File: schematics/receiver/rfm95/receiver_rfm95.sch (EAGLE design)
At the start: 47 parts, among them IC1 ATMEGA328P, Q1 16MHz, Q2 BC817-16SMD, U1 RFM95_LORA_MODULE, U2 AMS1117_3.3

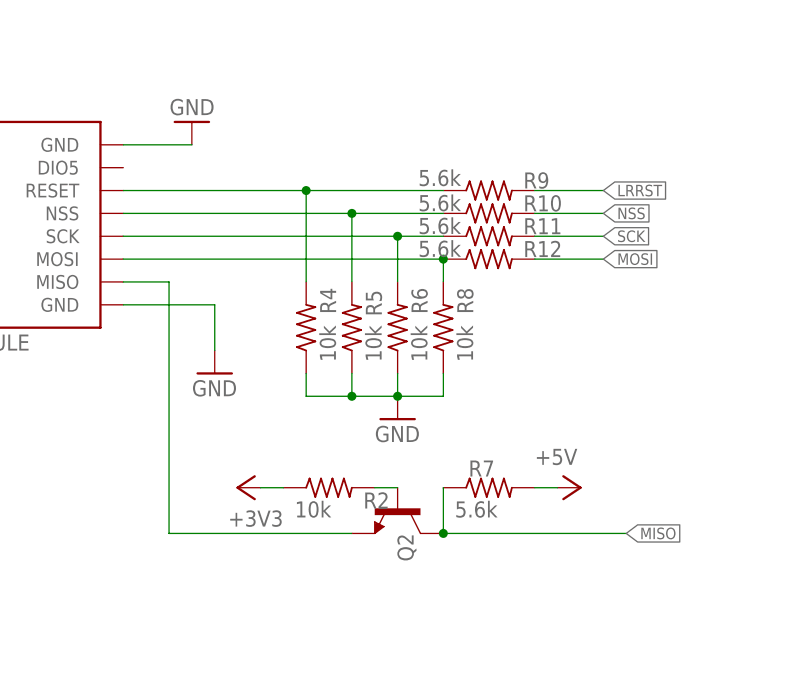
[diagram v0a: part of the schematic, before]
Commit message: Fixed incorrect resistor values
- Fixed incorrect resistor values in the level shifters.
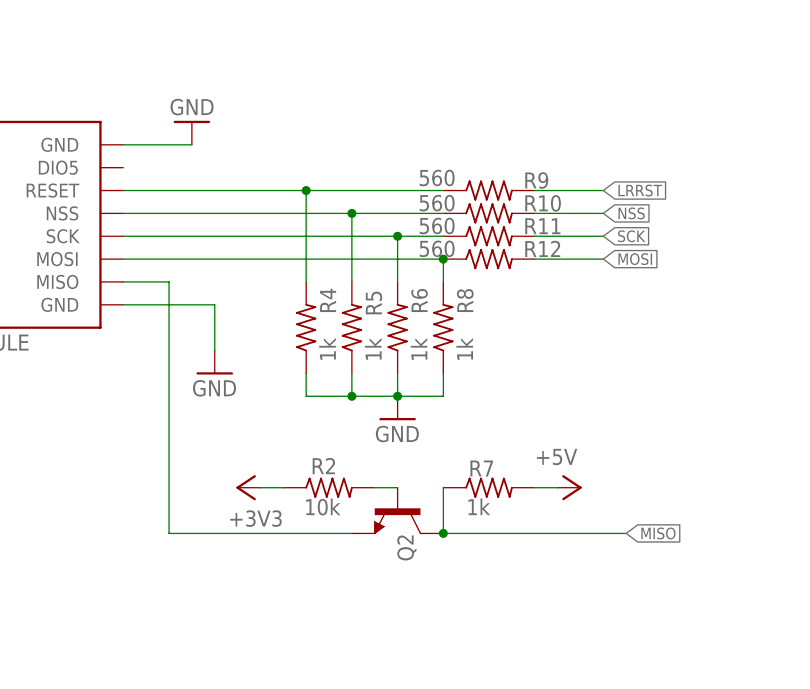
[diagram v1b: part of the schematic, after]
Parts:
- R10, R11, R12, R9: value 5.6k -> 560
- R4, R5, R6, R8: value 10k -> 1k
- R7: value 5.6k -> 1k
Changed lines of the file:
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@@
 <part name="P+9" library="supply1" deviceset="+5V" device=""/>
 <part name="P+4" library="supply1" deviceset="+5V" device=""/>
-<part name="R9" library="rcl" deviceset="R-US_" device="R0805" value="5.6k"/>
-<part name="R10" library="rcl" deviceset="R-US_" device="R0805" value="5.6k"/>
-<part name="R11" library="rcl" deviceset="R-US_" device="R0805" value="5.6k"/>
-<part name="R12" library="rcl" deviceset="R-US_" device="R0805" value="5.6k"/>
-<part name="R8" library="rcl" deviceset="R-US_" device="R0805" value="10k"/>
-<part name="R6" library="rcl" deviceset="R-US_" device="R0805" value="10k"/>
-<part name="R5" library="rcl" deviceset="R-US_" device="R0805" value="10k"/>
-<part name="R4" library="rcl" deviceset="R-US_" device="R0805" value="10k"/>
+<part name="R9" library="rcl" deviceset="R-US_" device="R0805" value="560"/>
+<part name="R10" library="rcl" deviceset="R-US_" device="R0805" value="560"/>
+<part name="R11" library="rcl" deviceset="R-US_" device="R0805" value="560"/>
+<part name="R12" library="rcl" deviceset="R-US_" device="R0805" value="560"/>
+<part name="R8" library="rcl" deviceset="R-US_" device="R0805" value="1k"/>
+<part name="R6" library="rcl" deviceset="R-US_" device="R0805" value="1k"/>
+<part name="R5" library="rcl" deviceset="R-US_" device="R0805" value="1k"/>
+<part name="R4" library="rcl" deviceset="R-US_" device="R0805" value="1k"/>
 <part name="GND8" library="supply1" deviceset="GND" device=""/>
 <part name="P+8" library="supply1" deviceset="+5V" device=""/>
 <part name="P+7" library="supply1" deviceset="+5V" device=""/>
 <part name="Q2" library="transistor-npn" deviceset="BC817*" device="SMD" technology="-16" value=""/>
-<part name="R7" library="rcl" deviceset="R-US_" device="R0805" value="5.6k"/>
+<part name="R7" library="rcl" deviceset="R-US_" device="R0805" value="1k"/>
 <part name="R2" library="rcl" deviceset="R-US_" device="R0805" value="10k"/>
 <part name="+3V32" library="supply1" deviceset="+3V3" device=""/>
@@
 <instance part="R7" gate="G$1" x="93.98" y="-35.56" smashed="yes">
 <attribute name="NAME" x="91.694" y="-34.3154" size="1.778" layer="95"/>
-<attribute name="VALUE" x="90.17" y="-38.862" size="1.778" layer="96"/>
+<attribute name="VALUE" x="91.44" y="-38.608" size="1.778" layer="96"/>
 </instance>
 <instance part="R2" gate="G$1" x="76.2" y="-35.56" smashed="yes">
-<attribute name="NAME" x="80.01" y="-37.8714" size="1.778" layer="95"/>
-<attribute name="VALUE" x="72.39" y="-38.862" size="1.778" layer="96"/>
+<attribute name="NAME" x="74.168" y="-34.0614" size="1.778" layer="95"/>
+<attribute name="VALUE" x="73.406" y="-38.608" size="1.778" layer="96"/>
 </instance>
 <instance part="+3V32" gate="G$1" x="66.04" y="-35.56" smashed="yes" rot="R90">
